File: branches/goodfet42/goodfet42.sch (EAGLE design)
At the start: 11 parts, among them U1 F261X---PM64, U2 FT232RL-BASICSSOP

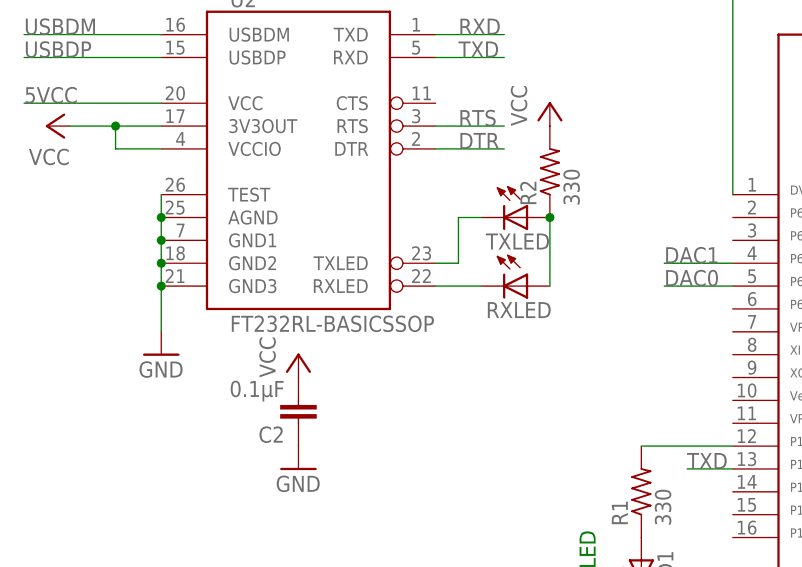
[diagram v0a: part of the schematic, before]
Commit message: Reinserted names, values in layout.
git-svn-id: https://svn.code.sf.net/p/goodfet/code@1316 12e2690d-a6be-4b82-a7b7-67c4a43b65c8
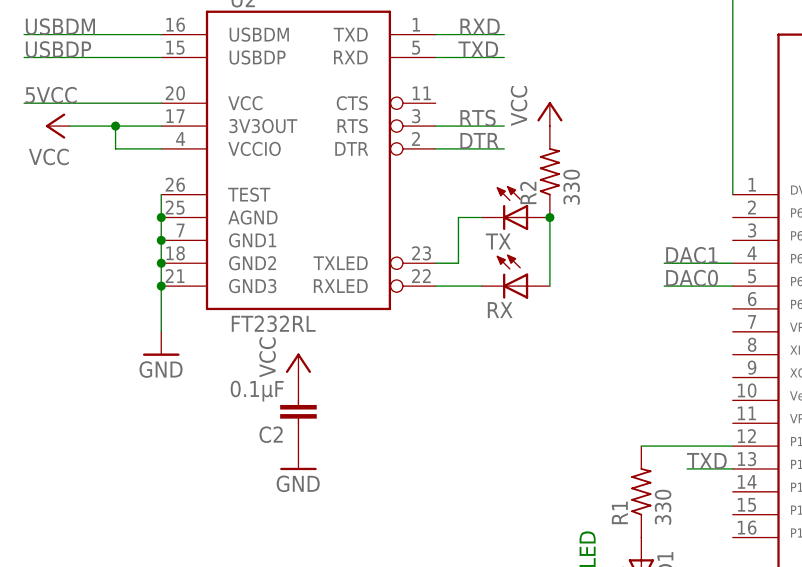
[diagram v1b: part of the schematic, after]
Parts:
- U1: value F261X---PM64 -> MSP430F2618TPM
- U2: value FT232RL-BASICSSOP -> FT232RL
- renumbered RXLED to RX, TXLED to TX
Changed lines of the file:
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@@
 <?xml version="1.0" encoding="utf-8"?>
 <!DOCTYPE eagle SYSTEM "eagle.dtd">
-<eagle version="6.2">
+<eagle version="6.3">
 <drawing>
 <settings>
@@
 <part name="LED1" library="led" deviceset="LED" device="CHIP-LED0603"/>
 <part name="GND1" library="supply1" deviceset="GND" device=""/>
-<part name="U2" library="SparkFun" deviceset="FT232RL-BASIC" device="SSOP"/>
+<part name="U2" library="SparkFun" deviceset="FT232RL-BASIC" device="SSOP" value="FT232RL"/>
 <part name="P+3" library="supply1" deviceset="VCC" device=""/>
 <part name="GND4" library="supply1" deviceset="GND" device=""/>
-<part name="RXLED" library="led" deviceset="LED" device="CHIP-LED0603"/>
-<part name="TXLED" library="led" deviceset="LED" device="CHIP-LED0603"/>
+<part name="RX" library="led" deviceset="LED" device="CHIP-LED0603"/>
+<part name="TX" library="led" deviceset="LED" device="CHIP-LED0603"/>
 <part name="P+4" library="supply1" deviceset="VCC" device=""/>
 <part name="R2" library="rcl" deviceset="R-US_" device="R0603" value="330"/>
@@
 <part name="GND5" library="supply1" deviceset="GND" device=""/>
 <part name="JTAG" library="con-lstb" deviceset="MA07-2" device=""/>
-<part name="U1" library="TI_MSP430_v13" deviceset="F261X---PM64" device=""/>
+<part name="U1" library="TI_MSP430_v13" deviceset="F261X---PM64" device="" value="MSP430F2618TPM"/>
 <part name="CN1" library="adafruit" deviceset="USB" device="MINIB"/>
 </parts>
@@
 <instance part="P+3" gate="VCC" x="-33.02" y="76.2" rot="R90"/>
 <instance part="GND4" gate="1" x="-20.32" y="50.8"/>
-<instance part="RXLED" gate="G$1" x="20.32" y="58.42" rot="R270"/>
-<instance part="TXLED" gate="G$1" x="20.32" y="66.04" rot="R270"/>
+<instance part="RX" gate="G$1" x="20.32" y="58.42" rot="R270"/>
+<instance part="TX" gate="G$1" x="20.32" y="66.04" rot="R270"/>
 <instance part="P+4" gate="VCC" x="22.86" y="78.74"/>
 <instance part="R2" gate="G$1" x="22.86" y="71.12" rot="R90"/>
@@
 <wire x1="10.16" y1="58.42" x2="15.24" y2="58.42" width="0.1524" layer="91"/>
 <pinref part="U2" gate="G$1" pin="RXLED"/>
-<pinref part="RXLED" gate="G$1" pin="C"/>
+<pinref part="RX" gate="G$1" pin="C"/>
 </segment>
 </net>
@@
 <wire x1="12.7" y1="66.04" x2="15.24" y2="66.04" width="0.1524" layer="91"/>
 <pinref part="U2" gate="G$1" pin="TXLED"/>
-<pinref part="TXLED" gate="G$1" pin="C"/>
+<pinref part="TX" gate="G$1" pin="C"/>
 </segment>
 </net>
@@
 <wire x1="22.86" y1="58.42" x2="22.86" y2="66.04" width="0.1524" layer="91"/>
 <junction x="22.86" y="66.04"/>
-<pinref part="RXLED" gate="G$1" pin="A"/>
-<pinref part="TXLED" gate="G$1" pin="A"/>
+<pinref part="RX" gate="G$1" pin="A"/>
+<pinref part="TX" gate="G$1" pin="A"/>
 <pinref part="R2" gate="G$1" pin="1"/>
 </segment>
